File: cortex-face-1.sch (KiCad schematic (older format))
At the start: 170 parts, among them J1 Conn_01x04, SW1 SW_Push, U1 Elite-C

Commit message: Changed footprints
Changed switch footprints to MX Only, no LED
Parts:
- MX_'"1, MX_,<1, MX_-_1, MX_.>1, MX_/1, MX_0)1, MX_1!1, MX_2@1, MX_3#1, MX_4$1, MX_5%1, MX_6^1, MX_7&1, MX_8*1, MX_9(1, MX_;:1, MX_=+1, MX_A1, MX_B1, MX_C1, MX_D1, MX_DOWN1, MX_E1, MX_END1, MX_F1, MX_F10, MX_F11, MX_F12, MX_F13, MX_F2, MX_F3, MX_F4, MX_F5, MX_F6, MX_F7, MX_F8, MX_F9, MX_FN1, MX_G1, MX_GRV1, MX_H1, MX_HOME1, MX_I1, MX_J1, MX_K1, MX_L1, MX_LEFT1, MX_M1, MX_N1, MX_O1, MX_P1, MX_PGDN1, MX_PGUP1, MX_Pn1, MX_Q1, MX_R1, MX_RIGHT1, MX_S1, MX_T1, MX_U1, MX_UP1, MX_V1, MX_W1, MX_X1, MX_Y1, MX_Z1, MX_[{1, MX_\|1, MX_]}1: footprint MX_Alps_Hybrid:MX-1U-NoLED -> MX_Only:MXOnly-1U-NoLED
- MX_BKSPC1: footprint MX_Alps_Hybrid:MX-2U-NoLED -> MX_Only:MXOnly-2U-NoLED
- MX_CAPS1, MX_RSHIFT1: footprint MX_Alps_Hybrid:MX-1.75U-NoLED -> MX_Only:MXOnly-1.75U-NoLED
- MX_DEL1, MX_TAB1: footprint MX_Alps_Hybrid:MX-1.5U-NoLED -> MX_Only:MXOnly-1.5U-NoLED
- MX_ENTER1: footprint MX_Alps_Hybrid:MX-2.25U-NoLED -> MX_Only:MXOnly-1U-NoLED
- MX_ESC1: footprint MX_Alps_Hybrid:MX-1.5U-NoLED -> MX_Only:MXOnly-1U-NoLED
- MX_LALT1, MX_LALT2, MX_LCTRL1, MX_LWIN1, MX_RCTRL1: footprint MX_Alps_Hybrid:MX-1.25U-NoLED -> MX_Only:MXOnly-1.25U-NoLED
- MX_LSHIFT1: footprint MX_Alps_Hybrid:MX-2.25U-NoLED -> MX_Only:MXOnly-2.25U-NoLED
- MX_SPC1: footprint MX_Alps_Hybrid:MX-6.25U-NoLED -> MX_Only:MXOnly-6.25U-NoLED

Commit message: Changed footprints
Footprints for non-standard switch sizes updated
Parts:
- MX_ENTER1: footprint MX_Only:MXOnly-1U-NoLED -> MX_Only:MXOnly-2.25U-NoLED
- MX_ESC1: footprint MX_Only:MXOnly-1U-NoLED -> MX_Only:MXOnly-1.5U-NoLED
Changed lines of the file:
@@
 F 0 "MX_ENTER1" H 9933 4523 60  0000 C CNN
 F 1 "MX-NoLED" H 9933 4449 20  0000 C CNN
-F 2 "MX_Only:MXOnly-1U-NoLED" H 9275 4275 60  0001 C CNN
+F 2 "MX_Only:MXOnly-2.25U-NoLED" H 9275 4275 60  0001 C CNN
 F 3 "" H 9275 4275 60  0001 C CNN
 	1    9900 4300
@@
 F 0 "MX_ESC1" H 6433 2123 60  0000 C CNN
 F 1 "MX-NoLED" H 6433 2049 20  0000 C CNN
-F 2 "MX_Only:MXOnly-1U-NoLED" H 5775 1875 60  0001 C CNN
+F 2 "MX_Only:MXOnly-1.5U-NoLED" H 5775 1875 60  0001 C CNN
 F 3 "" H 5775 1875 60  0001 C CNN
 	1    6400 1900

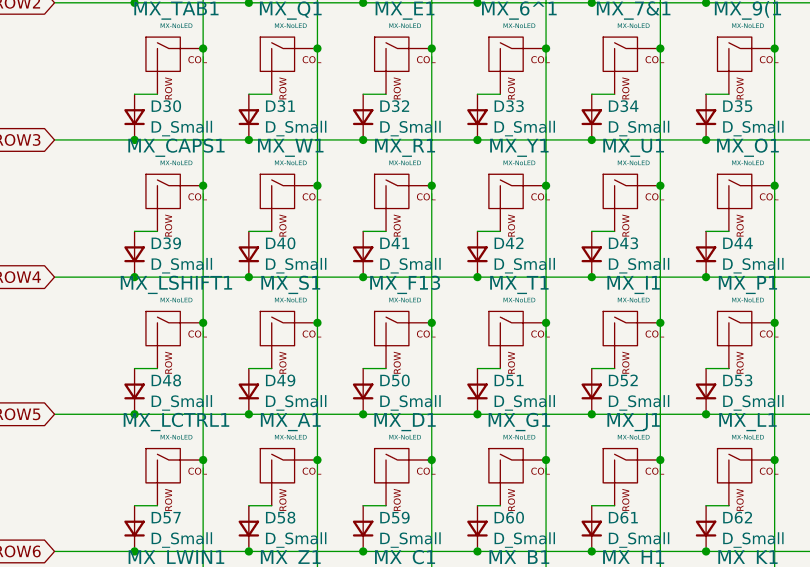
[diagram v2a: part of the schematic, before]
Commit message: Switches placed
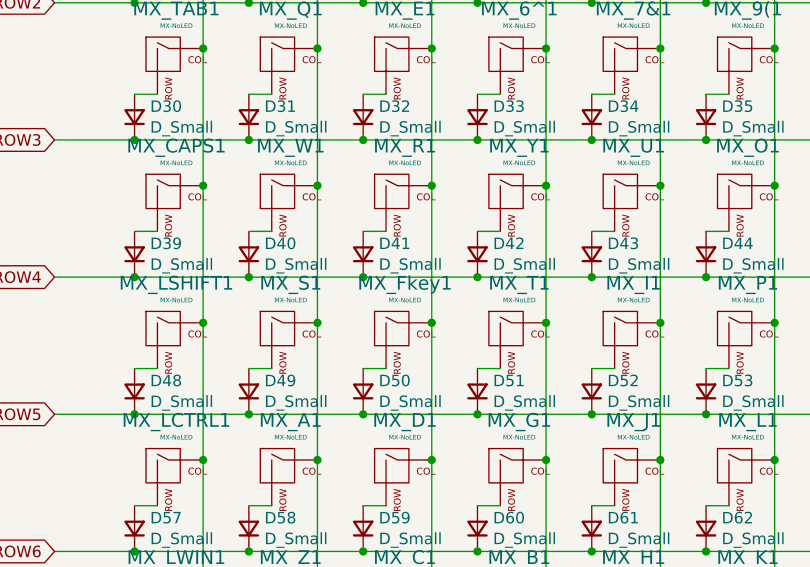
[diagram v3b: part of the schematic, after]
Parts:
- renumbered MX_F13 to MX_Fkey1
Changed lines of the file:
@@
 $EndComp
 $Comp
-L MX_Alps_Hybrid:MX-NoLED MX_F13
+L MX_Alps_Hybrid:MX-NoLED MX_Fkey1
 U 1 1 5DFFE048
 P 7400 4300
-F 0 "MX_F13" H 7433 4523 60  0000 C CNN
+F 0 "MX_Fkey1" H 7433 4523 60  0000 C CNN
 F 1 "MX-NoLED" H 7433 4449 20  0000 C CNN
 F 2 "MX_Only:MXOnly-1U-NoLED" H 6775 4275 60  0001 C CNN

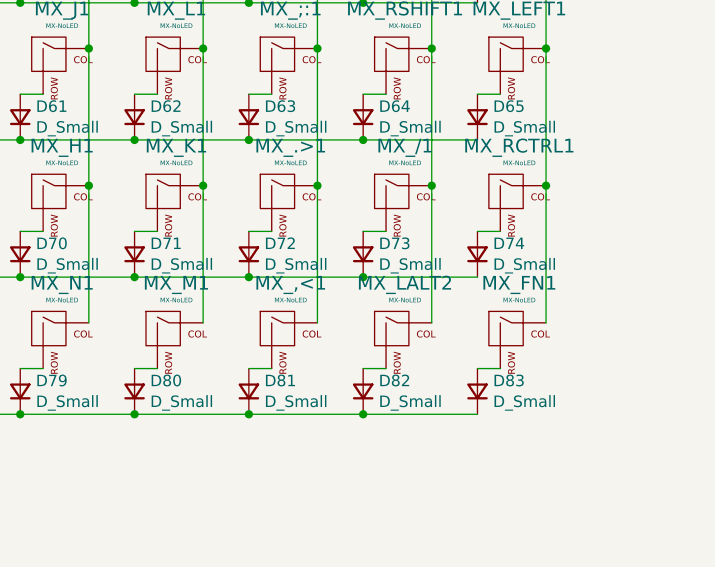
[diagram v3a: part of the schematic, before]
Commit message: Switches placed
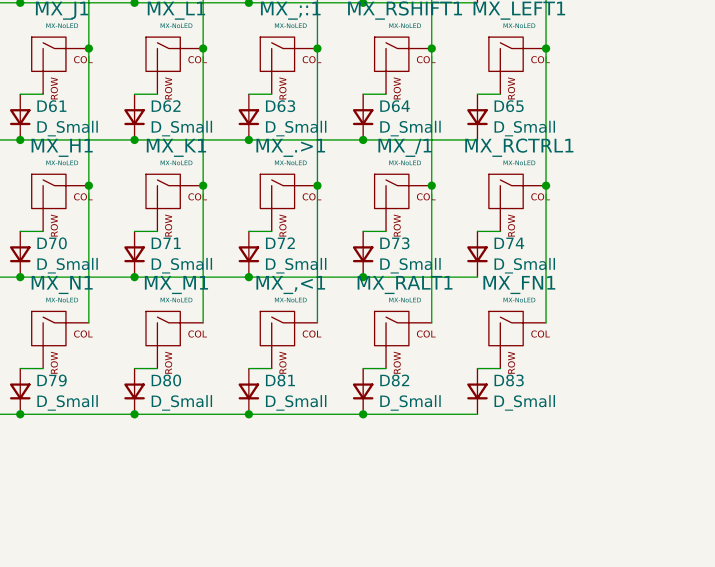
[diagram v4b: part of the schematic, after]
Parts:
- MX_RALT1: renamed from MX_LALT2; footprint MX_Only:MXOnly-1.25U-NoLED -> MX_Only:MXOnly-1U-NoLED
- MX_RCTRL1: footprint MX_Only:MXOnly-1.25U-NoLED -> MX_Only:MXOnly-1U-NoLED
- MX_\|1: footprint MX_Only:MXOnly-1U-NoLED -> MX_Only:MXOnly-1.5U-NoLED
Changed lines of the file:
@@
 F 0 "MX_RCTRL1" H 10433 5723 60  0000 C CNN
 F 1 "MX-NoLED" H 10433 5649 20  0000 C CNN
-F 2 "MX_Only:MXOnly-1.25U-NoLED" H 9775 5475 60  0001 C CNN
+F 2 "MX_Only:MXOnly-1U-NoLED" H 9775 5475 60  0001 C CNN
 F 3 "" H 9775 5475 60  0001 C CNN
 	1    10400 5500
@@
 	0    -1   -1   0
 $EndComp
-$Comp
-L MX_Alps_Hybrid:MX-NoLED MX_LALT2
-U 1 1 5E060A29
-P 9900 6100
-F 0 "MX_LALT2" H 9933 6323 60  0000 C CNN
-F 1 "MX-NoLED" H 9933 6249 20  0000 C CNN
-F 2 "MX_Only:MXOnly-1.25U-NoLED" H 9275 6075 60  0001 C CNN
-F 3 "" H 9275 6075 60  0001 C CNN
-	1    9900 6100
-	1    0    0    -1
-$EndComp
 Wire Wire Line
 	9750 5650 9850 5650
@@
 F 0 "MX_\\|1" H 9933 3323 60  0000 C CNN
 F 1 "MX-NoLED" H 9933 3249 20  0000 C CNN
-F 2 "MX_Only:MXOnly-1U-NoLED" H 9275 3075 60  0001 C CNN
+F 2 "MX_Only:MXOnly-1.5U-NoLED" H 9275 3075 60  0001 C CNN
 F 3 "" H 9275 3075 60  0001 C CNN
 	1    9900 3100
@@
 NoConn ~ 2600 7100
 NoConn ~ 2700 7100
+$Comp
+L MX_Alps_Hybrid:MX-NoLED MX_RALT1
+U 1 1 5E060A29
+P 9900 6100
+F 0 "MX_RALT1" H 9933 6323 60  0000 C CNN
+F 1 "MX-NoLED" H 9933 6249 20  0000 C CNN
+F 2 "MX_Only:MXOnly-1U-NoLED" H 9275 6075 60  0001 C CNN
+F 3 "" H 9275 6075 60  0001 C CNN
+	1    9900 6100
+	1    0    0    -1
+$EndComp
 $EndSCHEMATC
